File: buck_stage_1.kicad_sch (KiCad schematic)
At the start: 40 parts, among them J301 Conn_02x02_Odd_Even, Q301 MMBT5551, Q302 MMBT5551, Q303 LBSS84LT1G, U301 RT6365, U302 COS1333TR, U303 LMV321-TR

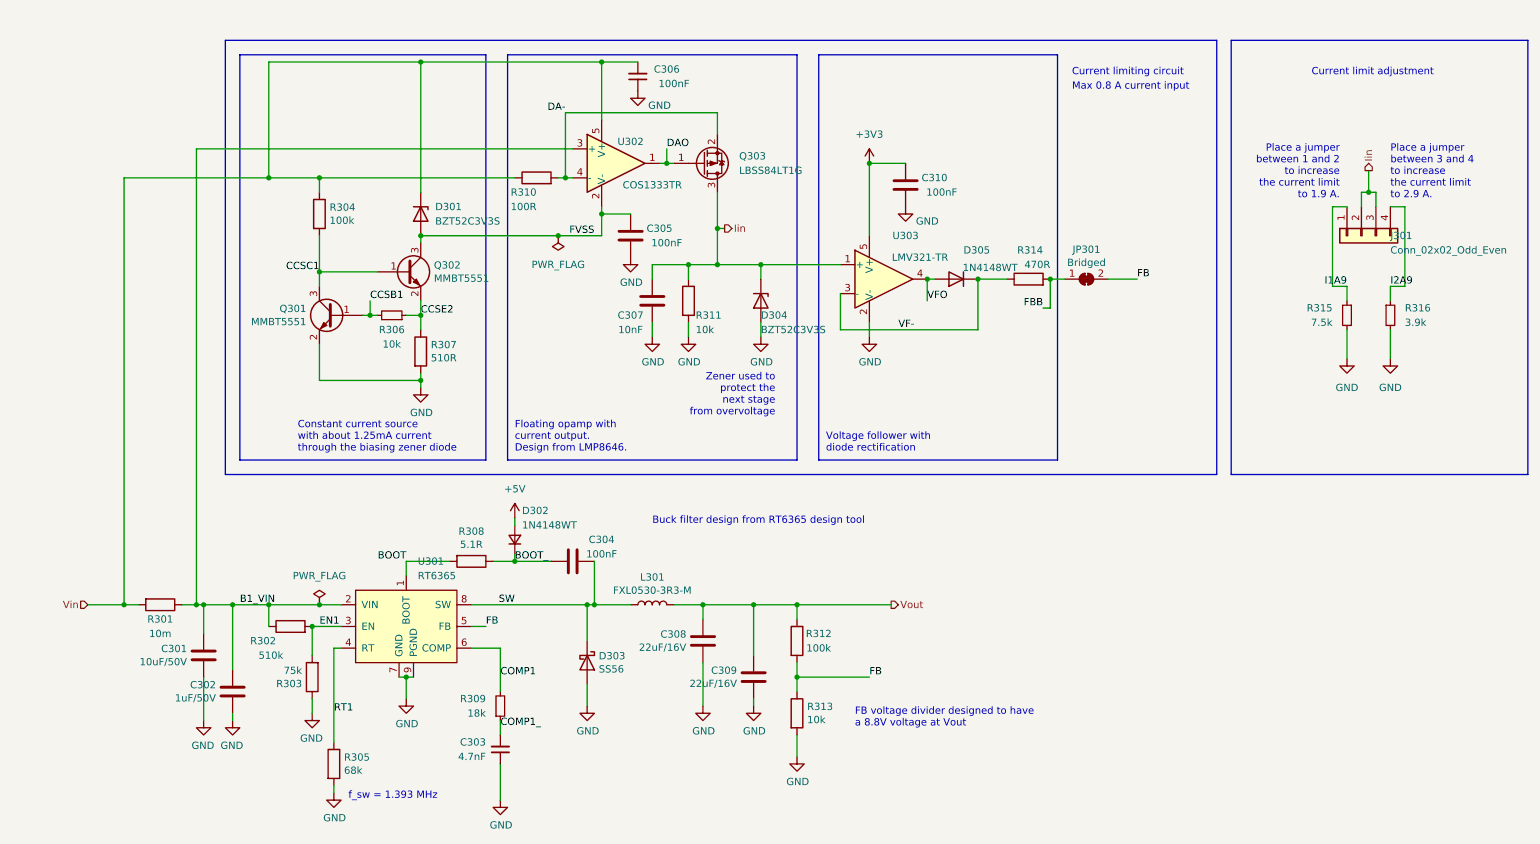
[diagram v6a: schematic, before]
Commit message: Replace "ideal diode" with Schottky & other changes
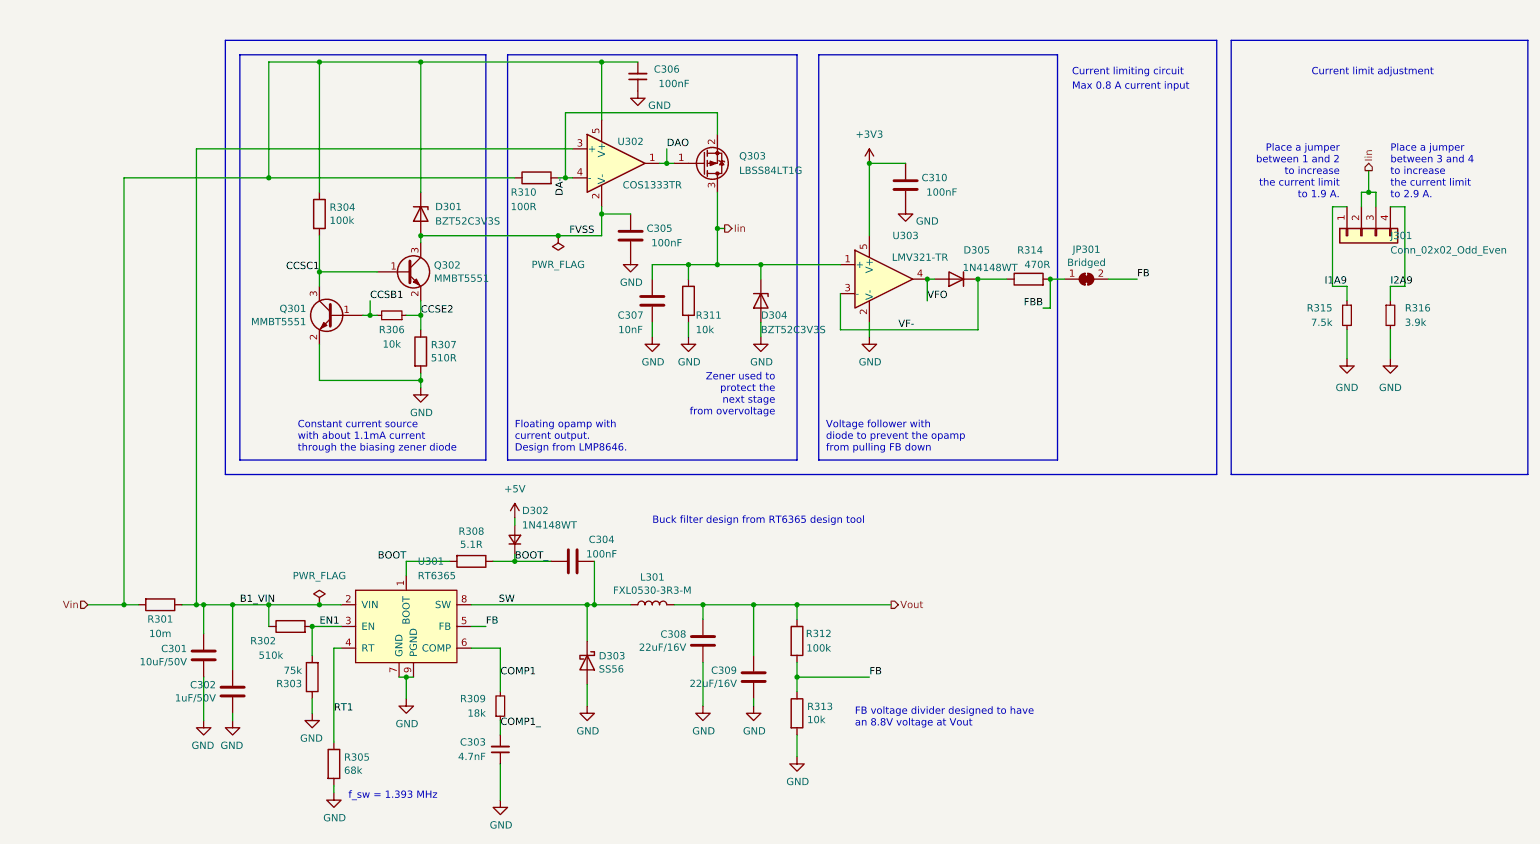
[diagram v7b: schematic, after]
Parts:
- JP301: footprint Jumper:SolderJumper-2_P1.3mm_Bridged2Bar_RoundedPad1.0x1.5mm -> Jumper:SolderJumper-2_P1.3mm_Bridged2Bar_Pad1.0x1.5mm
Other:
- note added: "Constant current source with about 1.1mA current through the biasing zener diode"
- note added: "FB voltage divider designed to have an 8.8V voltage at Vout"
- note added: "Voltage follower with diode to prevent the opamp from pulling FB down"
- note removed: "Constant current source with about 1.25mA current through the biasing zener diode"
- note removed: "FB voltage divider designed to have a 8.8V voltage at Vout"
- note removed: "Voltage follower with diode rectification"
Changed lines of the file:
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@@
   (title_block
     (title "Sailor Hat for Raspberry Pi")
-    (date "2022-10-14")
-    (rev "v2.0.0-alpha")
+    (date "2022-10-21")
+    (rev "v2.0.0-a1")
     (company "Hat Labs Ltd")
     (comment 1 "https://creativecommons.org/licenses/by/4.0")
@@
   (junction (at 196.85 64.77) (diameter 0) (color 0 0 0 0)
   )
-  (junction (at 68.58 46.99) (diameter 0) (color 0 0 0 0)
-  )
   (junction (at 68.58 121.92) (diameter 0) (color 0 0 0 0)
   )
@@
   (junction (at 165.1 44.45) (diameter 0) (color 0 0 0 0)
   )
+  (junction (at 68.58 26.67) (diameter 0) (color 0 0 0 0)
+  )
   (junction (at 111.76 46.99) (diameter 0) (color 0 0 0 0)
   )
@@
     (stroke (width 0) (type default) (color 0 0 0 0))
   )
+  (wire (pts (xy 68.58 26.67) (xy 68.58 49.53))
+    (stroke (width 0) (type default) (color 0 0 0 0))
+  )
   (wire (pts (xy 102.87 113.03) (xy 102.87 114.3))
     (stroke (width 0) (type default) (color 0 0 0 0))
@@
     (stroke (width 0) (type default) (color 0 0 0 0))
   )
+  (wire (pts (xy 138.43 62.23) (xy 146.05 62.23))
+    (stroke (width 0) (type default) (color 0 0 0 0))
+  )
+  (wire (pts (xy 71.12 154.94) (xy 71.12 153.67))
+    (stroke (width 0) (type default) (color 0 0 0 0))
+  )
+  (wire (pts (xy 138.43 55.88) (xy 139.7 55.88))
+    (stroke (width 0) (type default) (color 0 0 0 0))
+  )
+  (wire (pts (xy 184.15 73.66) (xy 160.02 73.66))
+    (stroke (width 0) (type default) (color 0 0 0 0))
+  )
+  (polyline (pts (xy 226.06 22.86) (xy 226.06 99.06))
+    (stroke (width 0) (type default) (color 0 0 0 0))
+  )
+  (polyline (pts (xy 280.67 99.06) (xy 228.6 99.06))
+    (stroke (width 0) (type default) (color 0 0 0 0))
+  )
+  (wire (pts (xy 100.33 129.54) (xy 95.25 129.54))
+    (stroke (width 0) (type default) (color 0 0 0 0))
+  )
+  (wire (pts (xy 152.4 134.62) (xy 165.1 134.62))
+    (stroke (width 0) (type default) (color 0 0 0 0))
+  )
+  (polyline (pts (xy 54.61 25.4) (xy 97.79 25.4))
+    (stroke (width 0) (type default) (color 0 0 0 0))
+  )
+  (polyline (pts (xy 97.79 25.4) (xy 97.79 96.52))
+    (stroke (width 0) (type default) (color 0 0 0 0))
+  )
+  (wire (pts (xy 146.05 64.77) (xy 146.05 62.23))
+    (stroke (width 0) (type default) (color 0 0 0 0))
+  )
+  (wire (pts (xy 53.34 121.92) (xy 59.69 121.92))
+    (stroke (width 0) (type default) (color 0 0 0 0))
+  )
+  (polyline (pts (xy 152.4 96.52) (xy 101.6 96.52))
+    (stroke (width 0) (type default) (color 0 0 0 0))
+  )
+  (wire (pts (xy 68.58 63.5) (xy 68.58 66.04))
+    (stroke (width 0) (type default) (color 0 0 0 0))
+  )
+  (polyline (pts (xy 198.12 25.4) (xy 198.12 96.52))
+    (stroke (width 0) (type default) (color 0 0 0 0))
+  )
+  (wire (pts (xy 129.54 41.91) (xy 129.54 44.45))
+    (stroke (width 0) (type default) (color 0 0 0 0))
+  )
+  (wire (pts (xy 86.36 57.15) (xy 86.36 58.42))
+    (stroke (width 0) (type default) (color 0 0 0 0))
+  )
+  (wire (pts (xy 144.78 130.81) (xy 144.78 121.92))
+    (stroke (width 0) (type default) (color 0 0 0 0))
+  )
+  (wire (pts (xy 83.82 71.12) (xy 86.36 71.12))
+    (stroke (width 0) (type default) (color 0 0 0 0))
+  )
+  (wire (pts (xy 248.92 52.07) (xy 246.38 52.07))
+    (stroke (width 0) (type default) (color 0 0 0 0))
+  )
+  (wire (pts (xy 86.36 71.12) (xy 86.36 68.58))
+    (stroke (width 0) (type default) (color 0 0 0 0))
+  )
+  (wire (pts (xy 135.89 132.08) (xy 135.89 139.7))
+    (stroke (width 0) (type default) (color 0 0 0 0))
+  )
+  (wire (pts (xy 67.31 138.43) (xy 67.31 140.97))
+    (stroke (width 0) (type default) (color 0 0 0 0))
+  )
   (wire (pts (xy 146.05 62.23) (xy 160.02 62.23))
     (stroke (width 0) (type default) (color 0 0 0 0))
   )
-  (wire (pts (xy 138.43 62.23) (xy 146.05 62.23))
-    (stroke (width 0) (type default) (color 0 0 0 0))
-  )
-  (wire (pts (xy 71.12 154.94) (xy 71.12 153.67))
-    (stroke (width 0) (type default) (color 0 0 0 0))
-  )
-  (wire (pts (xy 138.43 55.88) (xy 139.7 55.88))
-    (stroke (width 0) (type default) (color 0 0 0 0))
-  )
-  (wire (pts (xy 184.15 73.66) (xy 160.02 73.66))
-    (stroke (width 0) (type default) (color 0 0 0 0))
-  )
-  (polyline (pts (xy 226.06 22.86) (xy 226.06 99.06))
-    (stroke (width 0) (type default) (color 0 0 0 0))
-  )
-  (polyline (pts (xy 280.67 99.06) (xy 228.6 99.06))
-    (stroke (width 0) (type default) (color 0 0 0 0))
-  )
-  (wire (pts (xy 100.33 129.54) (xy 95.25 129.54))
-    (stroke (width 0) (type default) (color 0 0 0 0))
-  )
-  (wire (pts (xy 152.4 134.62) (xy 165.1 134.62))
-    (stroke (width 0) (type default) (color 0 0 0 0))
-  )
-  (polyline (pts (xy 54.61 25.4) (xy 97.79 25.4))
-    (stroke (width 0) (type default) (color 0 0 0 0))
-  )
-  (polyline (pts (xy 97.79 25.4) (xy 97.79 96.52))
-    (stroke (width 0) (type default) (color 0 0 0 0))
-  )
-  (wire (pts (xy 146.05 64.77) (xy 146.05 62.23))
-    (stroke (width 0) (type default) (color 0 0 0 0))
-  )
-  (wire (pts (xy 53.34 121.92) (xy 59.69 121.92))
-    (stroke (width 0) (type default) (color 0 0 0 0))
-  )
-  (polyline (pts (xy 152.4 96.52) (xy 101.6 96.52))
-    (stroke (width 0) (type default) (color 0 0 0 0))
-  )
-  (wire (pts (xy 68.58 63.5) (xy 68.58 66.04))
-    (stroke (width 0) (type default) (color 0 0 0 0))
-  )
-  (polyline (pts (xy 198.12 25.4) (xy 198.12 96.52))
-    (stroke (width 0) (type default) (color 0 0 0 0))
-  )
-  (wire (pts (xy 129.54 41.91) (xy 129.54 44.45))
-    (stroke (width 0) (type default) (color 0 0 0 0))
-  )
-  (wire (pts (xy 86.36 57.15) (xy 86.36 58.42))
-    (stroke (width 0) (type default) (color 0 0 0 0))
-  )
-  (wire (pts (xy 144.78 130.81) (xy 144.78 121.92))
-    (stroke (width 0) (type default) (color 0 0 0 0))
-  )
-  (wire (pts (xy 83.82 71.12) (xy 86.36 71.12))
-    (stroke (width 0) (type default) (color 0 0 0 0))
-  )
-  (wire (pts (xy 248.92 52.07) (xy 246.38 52.07))
-    (stroke (width 0) (type default) (color 0 0 0 0))
-  )
-  (wire (pts (xy 86.36 71.12) (xy 86.36 68.58))
-    (stroke (width 0) (type default) (color 0 0 0 0))
-  )
-  (wire (pts (xy 135.89 132.08) (xy 135.89 139.7))
-    (stroke (width 0) (type default) (color 0 0 0 0))
-  )
-  (wire (pts (xy 67.31 138.43) (xy 67.31 140.97))
-    (stroke (width 0) (type default) (color 0 0 0 0))
-  )
   (wire (pts (xy 152.4 148.59) (xy 152.4 144.78))
     (stroke (width 0) (type default) (color 0 0 0 0))
@@
     (stroke (width 0) (type default) (color 0 0 0 0))
   )
-  (wire (pts (xy 86.36 26.67) (xy 59.69 26.67))
+  (wire (pts (xy 86.36 26.67) (xy 68.58 26.67))
     (stroke (width 0) (type default) (color 0 0 0 0))
   )
@@
     (stroke (width 0) (type default) (color 0 0 0 0))
   )
+  (wire (pts (xy 68.58 26.67) (xy 59.69 26.67))
+    (stroke (width 0) (type default) (color 0 0 0 0))
+  )
   (wire (pts (xy 133.35 62.23) (xy 127 62.23))
     (stroke (width 0) (type default) (color 0 0 0 0))
@@
     (stroke (width 0) (type default) (color 0 0 0 0))
   )
-  (wire (pts (xy 68.58 46.99) (xy 102.87 46.99))
-    (stroke (width 0) (type default) (color 0 0 0 0))
-  )
-  (wire (pts (xy 59.69 46.99) (xy 68.58 46.99))
+  (wire (pts (xy 59.69 46.99) (xy 102.87 46.99))
     (stroke (width 0) (type default) (color 0 0 0 0))
   )
@@
     (stroke (width 0) (type default) (color 0 0 0 0))
   )
-  (wire (pts (xy 68.58 46.99) (xy 68.58 49.53))
-    (stroke (width 0) (type default) (color 0 0 0 0))
-  )
-  (text "Voltage follower with \ndiode rectification" (at 157.48 95.25 0)
-    (effects (font (size 1.27 1.27)) (justify left bottom))
-  )
-  (text "Constant current source\nwith about 1.25mA current\nthrough the biasing zener diode"
+  (text "Voltage follower with \ndiode to prevent the opamp\nfrom pulling FB down"
+    (at 157.48 95.25 0)
+    (effects (font (size 1.27 1.27)) (justify left bottom))
+  )
+  (text "Constant current source\nwith about 1.1mA current\nthrough the biasing zener diode"
     (at 64.77 95.25 0)
     (effects (font (size 1.27 1.27)) (justify left bottom))
@@
     (effects (font (size 1.27 1.27)) (justify right bottom))
   )
-  (text "FB voltage divider designed to have\na 8.8V voltage at Vout"
+  (text "FB voltage divider designed to have\nan 8.8V voltage at Vout"
     (at 162.56 143.51 0)
     (effects (font (size 1.27 1.27)) (justify left bottom))
@@
     (effects (font (size 1.27 1.27)) (justify right bottom))
   )
-  (label "DA-" (at 111.76 35.56 180)
+  (label "DA-" (at 111.76 46.99 270)
     (effects (font (size 1.27 1.27)) (justify right bottom))
   )
@@
     (property "Reference" "JP301" (id 0) (at 203.2 59.563 0))
     (property "Value" "Bridged" (id 1) (at 203.2 61.8744 0))
-    (property "Footprint" "Jumper:SolderJumper-2_P1.3mm_Bridged2Bar_RoundedPad1.0x1.5mm" (id 2) (at 203.2 64.77 0)
-      (effects (font (size 1.27 1.27)) hide)
-    )
+    (property "Footprint" "Jumper:SolderJumper-2_P1.3mm_Bridged2Bar_Pad1.0x1.5mm" (id 2) (at 203.2 64.77 0)
+      (effects (font (size 1.27 1.27)) hide)
+    )

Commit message: Redesign the EMI input filter
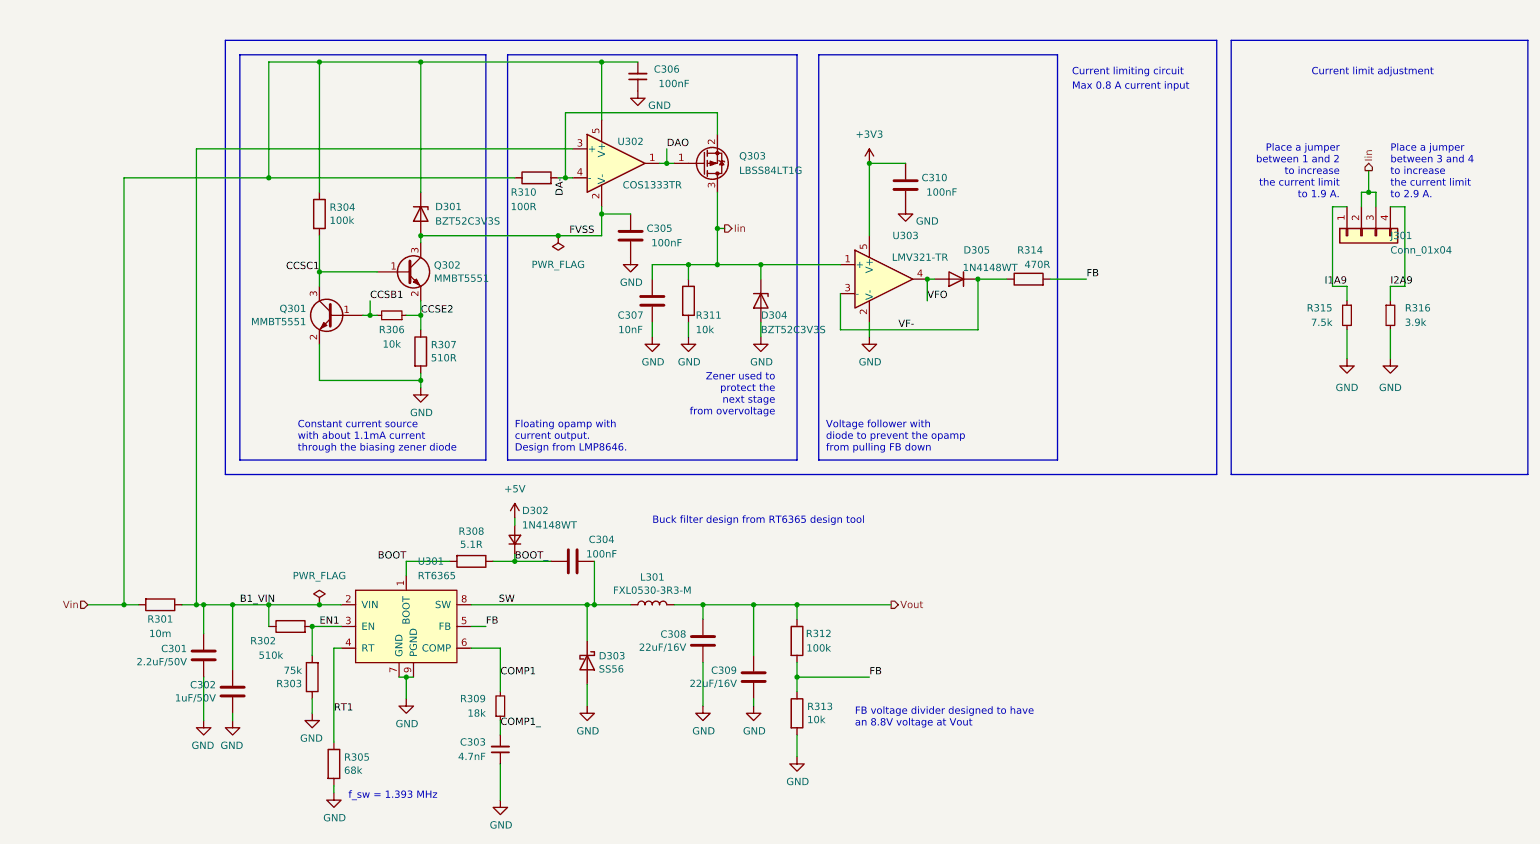
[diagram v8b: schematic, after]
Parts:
- removed JP301: Bridged, Jumper:SolderJumper-2_P1.3mm_Bridged2Bar_Pad1.0x1.5mm, symbol Jumper:SolderJumper_2_Bridged
- C301: value 10uF/50V -> 2.2uF/50V; LCSC C13585 -> C50254
- D301: LCSC C188195 -> C173439
- D304: LCSC C2932762 -> C173439
- J301: value Conn_02x02_Odd_Even -> Conn_01x04; LCSC C492419 -> C152150
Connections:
- net FBB is gone; now on net FB: R314.2
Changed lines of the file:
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@@
   (junction (at 86.36 26.67) (diameter 0) (color 0 0 0 0)
   )
-  (junction (at 196.85 64.77) (diameter 0) (color 0 0 0 0)
-  )
   (junction (at 68.58 121.92) (diameter 0) (color 0 0 0 0)
   )
@@
     (stroke (width 0) (type default) (color 0 0 0 0))
   )
+  (wire (pts (xy 196.85 64.77) (xy 203.2 64.77))
+    (stroke (width 0) (type default) (color 0 0 0 0))
+  )
   (polyline (pts (xy 52.07 22.86) (xy 52.07 99.06))
     (stroke (width 0) (type default) (color 0 0 0 0))
@@
     (stroke (width 0) (type default) (color 0 0 0 0))
   )
-  (wire (pts (xy 207.01 64.77) (xy 212.09 64.77))
-    (stroke (width 0) (type default) (color 0 0 0 0))
-  )
   (wire (pts (xy 133.35 62.23) (xy 133.35 64.77))
     (stroke (width 0) (type default) (color 0 0 0 0))
@@
     (stroke (width 0) (type default) (color 0 0 0 0))
   )
-  (wire (pts (xy 195.58 69.85) (xy 196.85 69.85))
-    (stroke (width 0) (type default) (color 0 0 0 0))
-  )
   (wire (pts (xy 144.78 138.43) (xy 144.78 139.7))
     (stroke (width 0) (type default) (color 0 0 0 0))
@@
     (stroke (width 0) (type default) (color 0 0 0 0))
   )
-  (wire (pts (xy 196.85 64.77) (xy 199.39 64.77))
-    (stroke (width 0) (type default) (color 0 0 0 0))
-  )
   (polyline (pts (xy 101.6 25.4) (xy 101.6 96.52))
     (stroke (width 0) (type default) (color 0 0 0 0))
@@
   )
   (polyline (pts (xy 54.61 25.4) (xy 54.61 96.52))
-    (stroke (width 0) (type default) (color 0 0 0 0))
-  )
-  (wire (pts (xy 196.85 69.85) (xy 196.85 64.77))
     (stroke (width 0) (type default) (color 0 0 0 0))
   )
@@
     (effects (font (size 1.27 1.27)) (justify left bottom))
   )
-  (label "FB" (at 212.09 64.77 0)
+  (label "FB" (at 203.2 64.77 0)
     (effects (font (size 1.27 1.27)) (justify left bottom))
   )
   (label "B1_VIN" (at 54.61 121.92 0)
     (effects (font (size 1.27 1.27)) (justify left bottom))
-  )
-  (label "FBB" (at 195.58 69.85 180)
-    (effects (font (size 1.27 1.27)) (justify right bottom))
   )
   (label "VFO" (at 175.26 68.58 0)
@@
       (effects (font (size 1.27 1.27)) (justify left))
     )
-    (property "Value" "10uF/50V" (id 1) (at 45.339 131.953 0)
+    (property "Value" "2.2uF/50V" (id 1) (at 45.339 131.953 0)
       (effects (font (size 1.27 1.27)) (justify left))
     )
@@
       (effects (font (size 1.27 1.27)) hide)
     )
-    (property "LCSC" "C13585" (id 4) (at 48.26 130.81 0)
+    (property "LCSC" "C50254" (id 4) (at 48.26 130.81 0)
       (effects (font (size 1.27 1.27)) hide)
     )
@@
     )
     (pin "1")
-  )
-  (symbol (lib_id "Jumper:SolderJumper_2_Bridged") (at 203.2 64.77 0) (unit 1)
-    (in_bom yes) (on_board yes)
-    (property "Reference" "JP301" (id 0) (at 203.2 59.563 0))
-    (property "Value" "Bridged" (id 1) (at 203.2 61.8744 0))
-    (property "Footprint" "Jumper:SolderJumper-2_P1.3mm_Bridged2Bar_Pad1.0x1.5mm" (id 2) (at 203.2 64.77 0)
-      (effects (font (size 1.27 1.27)) hide)
-    )
-    (property "Datasheet" "~" (id 3) (at 203.2 64.77 0)
-      (effects (font (size 1.27 1.27)) hide)
-    )
-    (pin "1")
-    (pin "2")
   )
   (symbol (lib_id "Device:C") (at 53.34 137.16 0) (mirror y) (unit 1)
@@
       (effects (font (size 1.27 1.27)) hide)
     )
-    (property "LCSC" "C188195" (id 4) (at 86.36 53.34 90)
+    (property "LCSC" "C173439" (id 4) (at 86.36 53.34 90)
       (effects (font (size 1.27 1.27)) hide)
     )
@@
       (effects (font (size 1.27 1.27)) (justify right))
     )
-    (property "Value" "Conn_02x02_Odd_Even" (id 1) (at 256.54 59.6899 90)
+    (property "Value" "Conn_01x04" (id 1) (at 256.54 59.6899 90)
       (effects (font (size 1.27 1.27)) (justify right))
     )
@@
       (effects (font (size 1.27 1.27)) hide)
     )
-    (property "LCSC" "C492419" (id 4) (at 251.46 57.15 90)
+    (property "LCSC" "C152150" (id 4) (at 251.46 57.15 90)
       (effects (font (size 1.27 1.27)) hide)
     )
@@
       (effects (font (size 1.27 1.27)) hide)
     )
-    (property "LCSC" "C2932762" (id 4) (at 146.05 68.58 90)
-      (effects (font (size 1.27 1.27)) hide)
-    )
+    (property "LCSC" "C173439" (id 4) (at 146.05 68.58 90)
+      (effects (font (size 1.27 1.27)) hide)
+    )
